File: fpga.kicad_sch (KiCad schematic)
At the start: 10 parts, among them U10 P0082_BOTTOMMOUNT, Y1 XLL735080.000000I

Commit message: Start working on ERC, properly annotate DNP elements
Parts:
- R56, R58, R72: now not fitted
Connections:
- no-connect marks 1 -> 22
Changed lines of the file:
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@@
 	)
 	(no_connect
+		(at 125.73 95.25)
+	)
+	(no_connect
+		(at 125.73 135.89)
+	)
+	(no_connect
+		(at 125.73 128.27)
+	)
+	(no_connect
+		(at 80.01 49.53)
+	)
+	(no_connect
+		(at 125.73 130.81)
+	)
+	(no_connect
+		(at 80.01 100.33)
+	)
+	(no_connect
+		(at 125.73 90.17)
+	)
+	(no_connect
 		(at 217.17 59.69)
 	)
+	(no_connect
+		(at 125.73 92.71)
+	)
+	(no_connect
+		(at 125.73 87.63)
+	)
+	(no_connect
+		(at 125.73 120.65)
+	)
+	(no_connect
+		(at 80.01 90.17)
+	)
+	(no_connect
+		(at 80.01 46.99)
+	)
+	(no_connect
+		(at 125.73 123.19)
+	)
+	(no_connect
+		(at 125.73 62.23)
+	)
+	(no_connect
+		(at 80.01 123.19)
+	)
+	(no_connect
+		(at 80.01 92.71)
+	)
+	(no_connect
+		(at 125.73 64.77)
+	)
+	(no_connect
+		(at 125.73 46.99)
+	)
+	(no_connect
+		(at 125.73 125.73)
+	)
+	(no_connect
+		(at 80.01 95.25)
+	)
+	(no_connect
+		(at 125.73 85.09)
+	)
 	(bus_entry
 		(at 181.61 106.68)
@@
 		(in_bom yes)
 		(on_board yes)
-		(dnp no)
+		(dnp yes)
 		(fields_autoplaced yes)
 		(property "Reference" "R72"
@@
 		(in_bom yes)
 		(on_board yes)
-		(dnp no)
+		(dnp yes)
 		(property "Reference" "R56"
 			(at 138.176 40.64 90)
@@
 		(in_bom yes)
 		(on_board yes)
-		(dnp no)
+		(dnp yes)
 		(property "Reference" "R58"
 			(at 138.176 114.3 90)

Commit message: Fix ERC
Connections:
- net +3.3V is gone; now on net +3V3: C140.1, R72.1, Y1.6 (VDD)
- net ADC_B_10: no longer U10.JP2_33 (GPIO_126)
- net ADC_B_11: no longer U10.JP2_35 (GPIO_128)
- net OVERFLOW: now reaches U10.JP1_35 (GPIO_028)
- new net ADC_B_12: U10.JP2_33 (GPIO_126)
- new net ADC_B_13: U10.JP2_35 (GPIO_128)
- no-connect marks 22 -> 21
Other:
- moved on the sheet: R55, R56, R57, R58, R72

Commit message: Add all footprints
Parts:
- renumbered C140 to C100, R180 to R58, R181 to R59, R55 to R60, R56 to R61, R57 to R62, R58 to R63, R72 to R64
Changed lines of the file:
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@@
 		(on_board yes)
 		(dnp no)
-		(property "Reference" "R181"
+		(property "Reference" "R59"
 			(at 70.866 86.36 90)
 			(effects
@@
 			(project "DigitalOsciloscope"
 				(path "/553deb7b-4100-40fe-99d2-0c7b4b56aad2/3a7288c4-cf21-495b-9b8e-7b87b52ff1d8"
-					(reference "R181")
+					(reference "R59")
 					(unit 1)
 				)
@@
 		(dnp no)
 		(fields_autoplaced yes)
-		(property "Reference" "#PWR056"
+		(property "Reference" "#PWR0143"
 			(at 161.29 41.91 0)
 			(effects
@@
 			(project "DigitalOsciloscope"
 				(path "/553deb7b-4100-40fe-99d2-0c7b4b56aad2/3a7288c4-cf21-495b-9b8e-7b87b52ff1d8"
-					(reference "#PWR056")
+					(reference "#PWR0143")
 					(unit 1)
 				)
@@
 		(dnp no)
 		(fields_autoplaced yes)
-		(property "Reference" "#PWR0243"
+		(property "Reference" "#PWR0148"
 			(at 236.22 72.39 0)
 			(effects
@@
 			(project ""
 				(path "/553deb7b-4100-40fe-99d2-0c7b4b56aad2/3a7288c4-cf21-495b-9b8e-7b87b52ff1d8"
-					(reference "#PWR0243")
+					(reference "#PWR0148")
 					(unit 1)
 				)
@@
 		(dnp no)
 		(fields_autoplaced yes)
-		(property "Reference" "#PWR054"
+		(property "Reference" "#PWR0144"
 			(at 161.29 115.57 0)
 			(effects
@@
 			(project ""
 				(path "/553deb7b-4100-40fe-99d2-0c7b4b56aad2/3a7288c4-cf21-495b-9b8e-7b87b52ff1d8"
-					(reference "#PWR054")
+					(reference "#PWR0144")
 					(unit 1)
 				)
@@
 		(on_board yes)
 		(dnp no)
-		(property "Reference" "R180"
+		(property "Reference" "R58"
 			(at 70.866 83.82 90)
 			(effects
@@
 			(project "DigitalOsciloscope"
 				(path "/553deb7b-4100-40fe-99d2-0c7b4b56aad2/3a7288c4-cf21-495b-9b8e-7b87b52ff1d8"
-					(reference "R180")
+					(reference "R58")
 					(unit 1)
 				)
@@
 		(dnp no)
 		(fields_autoplaced yes)
-		(property "Reference" "#PWR0160"
+		(property "Reference" "#PWR0145"
 			(at 176.53 58.42 0)
 			(effects
@@
 			(project "DigitalOsciloscope"
 				(path "/553deb7b-4100-40fe-99d2-0c7b4b56aad2/3a7288c4-cf21-495b-9b8e-7b87b52ff1d8"
-					(reference "#PWR0160")
+					(reference "#PWR0145")
 					(unit 1)
 				)
@@
 		(dnp no)
 		(fields_autoplaced yes)
-		(property "Reference" "#FLG034"
+		(property "Reference" "#FLG024"
 			(at 134.62 111.125 0)
 			(effects
@@
 			(project "DigitalOsciloscope"
 				(path "/553deb7b-4100-40fe-99d2-0c7b4b56aad2/3a7288c4-cf21-495b-9b8e-7b87b52ff1d8"
-					(reference "#FLG034")
+					(reference "#FLG024")
 					(unit 1)
 				)
@@
 		(dnp no)
 		(fields_autoplaced yes)
-		(property "Reference" "#PWR053"
+		(property "Reference" "#PWR0142"
 			(at 156.21 115.57 0)
 			(effects
@@
 			(project ""
 				(path "/553deb7b-4100-40fe-99d2-0c7b4b56aad2/3a7288c4-cf21-495b-9b8e-7b87b52ff1d8"
-					(reference "#PWR053")
+					(reference "#PWR0142")
 					(unit 1)
 				)
@@
 		(dnp yes)
 		(fields_autoplaced yes)
-		(property "Reference" "R72"
+		(property "Reference" "R64"
 			(at 182.88 50.8 90)
 			(effects
@@
 			(project ""
 				(path "/553deb7b-4100-40fe-99d2-0c7b4b56aad2/3a7288c4-cf21-495b-9b8e-7b87b52ff1d8"
-					(reference "R72")
+					(reference "R64")
 					(unit 1)
 				)
@@
 		(dnp no)
 		(fields_autoplaced yes)
-		(property "Reference" "#PWR057"
+		(property "Reference" "#PWR0140"
 			(at 127 185.42 0)
 			(effects
@@
 			(project ""
 				(path "/553deb7b-4100-40fe-99d2-0c7b4b56aad2/3a7288c4-cf21-495b-9b8e-7b87b52ff1d8"
-					(reference "#PWR057")
+					(reference "#PWR0140")
 					(unit 1)
 				)
@@
 		(on_board yes)
 		(dnp no)
-		(property "Reference" "#FLG06"
+		(property "Reference" "#FLG023"
 			(at 134.62 43.815 0)
 			(effects
@@
 			(project "DigitalOsciloscope"
 				(path "/553deb7b-4100-40fe-99d2-0c7b4b56aad2/3a7288c4-cf21-495b-9b8e-7b87b52ff1d8"
-					(reference "#FLG06")
+					(reference "#FLG023")
 					(unit 1)
 				)
@@
 		(dnp no)
 		(fields_autoplaced yes)
-		(property "Reference" "#FLG035"
+		(property "Reference" "#FLG025"
 			(at 134.62 117.475 0)
 			(effects
@@
 			(project "DigitalOsciloscope"
 				(path "/553deb7b-4100-40fe-99d2-0c7b4b56aad2/3a7288c4-cf21-495b-9b8e-7b87b52ff1d8"
-					(reference "#FLG035")
+					(reference "#FLG025")
 					(unit 1)
 				)
@@
 		(dnp no)
 		(fields_autoplaced yes)
-		(property "Reference" "#PWR0244"
+		(property "Reference" "#PWR0146"
 			(at 187.96 69.85 0)
 			(effects
@@
 			(project "DigitalOsciloscope"
 				(path "/553deb7b-4100-40fe-99d2-0c7b4b56aad2/3a7288c4-cf21-495b-9b8e-7b87b52ff1d8"
-					(reference "#PWR0244")
+					(reference "#PWR0146")
 					(unit 1)
 				)
@@
 		(dnp no)
 		(fields_autoplaced yes)
-		(property "Reference" "#PWR058"
+		(property "Reference" "#PWR0139"
 			(at 127 109.22 0)
 			(effects
@@
 			(project "DigitalOsciloscope"
 				(path "/553deb7b-4100-40fe-99d2-0c7b4b56aad2/3a7288c4-cf21-495b-9b8e-7b87b52ff1d8"
-					(reference "#PWR058")
+					(reference "#PWR0139")
 					(unit 1)
 				)
@@
 		(on_board yes)
 		(dnp no)
-		(property "Reference" "R55"
+		(property "Reference" "R60"
 			(at 148.336 38.1 90)
 			(effects
@@
 			(project "DigitalOsciloscope"
 				(path "/553deb7b-4100-40fe-99d2-0c7b4b56aad2/3a7288c4-cf21-495b-9b8e-7b87b52ff1d8"
-					(reference "R55")
+					(reference "R60")
 					(unit 1)
 				)
@@
 		(dnp no)
 		(fields_autoplaced yes)
-		(property "Reference" "#PWR059"
+		(property "Reference" "#PWR0147"
 			(at 236.22 58.42 0)
 			(effects
@@
 			(project "DigitalOsciloscope"
 				(path "/553deb7b-4100-40fe-99d2-0c7b4b56aad2/3a7288c4-cf21-495b-9b8e-7b87b52ff1d8"
-					(reference "#PWR059")
+					(reference "#PWR0147")
 					(unit 1)
 				)
@@
 		(dnp no)
 		(fields_autoplaced yes)
-		(property "Reference" "#PWR055"
+		(property "Reference" "#PWR0141"
 			(at 156.21 41.91 0)
 			(effects
@@
 			(project "DigitalOsciloscope"
 				(path "/553deb7b-4100-40fe-99d2-0c7b4b56aad2/3a7288c4-cf21-495b-9b8e-7b87b52ff1d8"
-					(reference "#PWR055")
+					(reference "#PWR0141")
 					(unit 1)
 				)
@@
 		(on_board yes)
 		(dnp no)
-		(property "Reference" "R57"
+		(property "Reference" "R62"
 			(at 148.336 111.76 90)
 			(effects
@@
 			(project "DigitalOsciloscope"
 				(path "/553deb7b-4100-40fe-99d2-0c7b4b56aad2/3a7288c4-cf21-495b-9b8e-7b87b52ff1d8"
-					(reference "R57")
+					(reference "R62")
 					(unit 1)
 				)
@@
 		(dnp no)
 		(fields_autoplaced yes)
-		(property "Reference" "#FLG05"
+		(property "Reference" "#FLG022"
 			(at 134.62 37.465 0)
 			(effects
@@
 			(project ""
 				(path "/553deb7b-4100-40fe-99d2-0c7b4b56aad2/3a7288c4-cf21-495b-9b8e-7b87b52ff1d8"
-					(reference "#FLG05")
+					(reference "#FLG022")
 					(unit 1)
 				)
@@
 		(on_board yes)
 		(dnp yes)
-		(property "Reference" "R56"
+		(property "Reference" "R61"
 			(at 148.336 40.64 90)
 			(effects
@@
 			(project "DigitalOsciloscope"
 				(path "/553deb7b-4100-40fe-99d2-0c7b4b56aad2/3a7288c4-cf21-495b-9b8e-7b87b52ff1d8"
-					(reference "R56")
+					(reference "R61")
 					(unit 1)
 				)
@@
 		(on_board yes)
 		(dnp yes)
-		(property "Reference" "R58"
+		(property "Reference" "R63"
 			(at 148.336 114.3 90)
 			(effects
@@
 			(project "DigitalOsciloscope"
 				(path "/553deb7b-4100-40fe-99d2-0c7b4b56aad2/3a7288c4-cf21-495b-9b8e-7b87b52ff1d8"
-					(reference "R58")
+					(reference "R63")
 					(unit 1)
 				)
@@
 		(dnp no)
 		(fields_autoplaced yes)
-		(property "Reference" "C140"
+		(property "Reference" "C100"
 			(at 240.03 60.9599 0)
 			(effects
@@
 			(project ""
 				(path "/553deb7b-4100-40fe-99d2-0c7b4b56aad2/3a7288c4-cf21-495b-9b8e-7b87b52ff1d8"
-					(reference "C140")
-					(unit 1)
-				)
+					(reference "C100")
+					(unit 1)
+				)

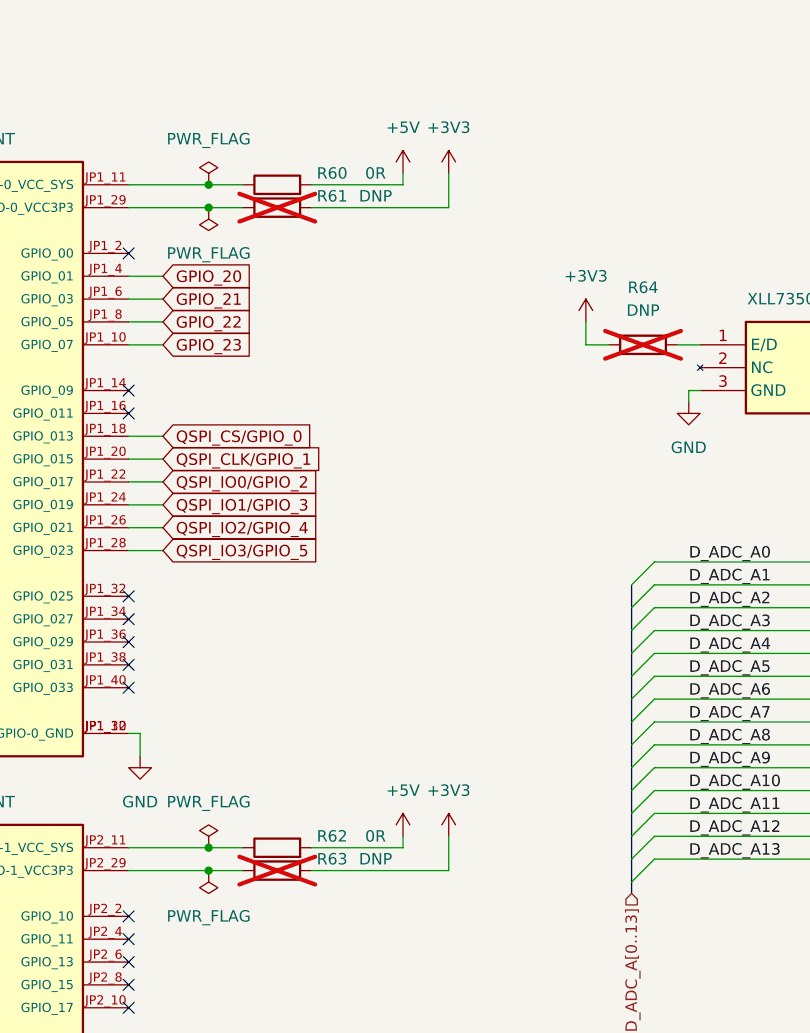
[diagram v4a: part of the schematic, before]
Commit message: Apply changes after review, left to fix: comparator histeresis, PSU missing lines?
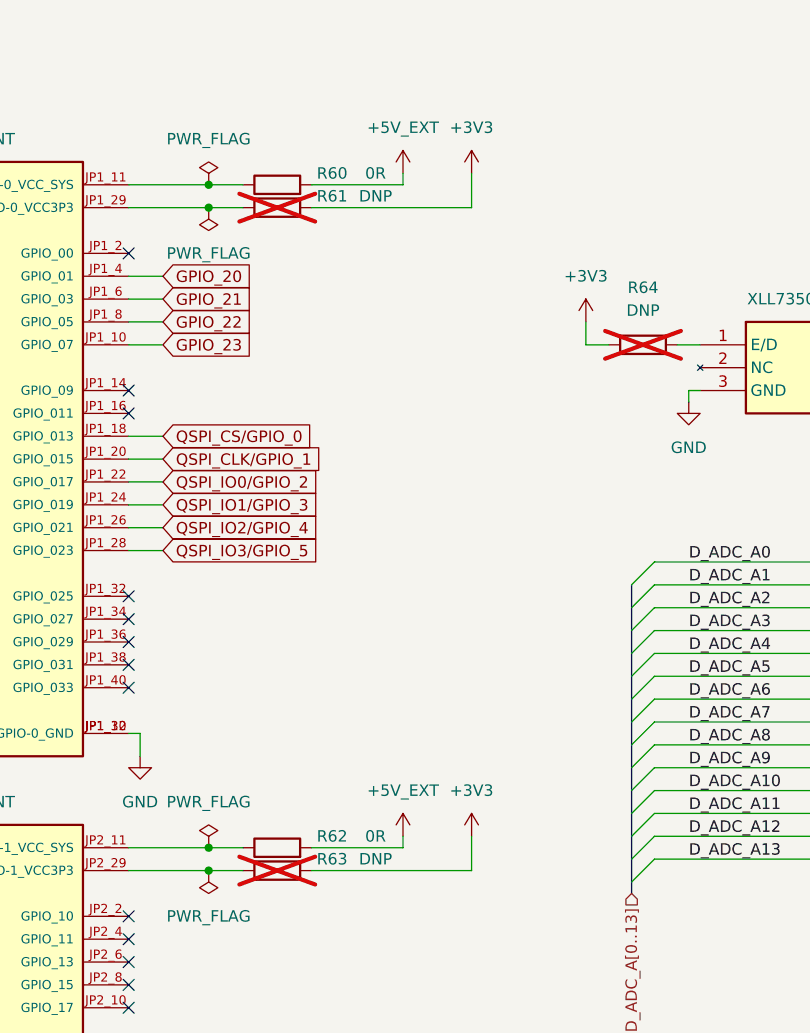
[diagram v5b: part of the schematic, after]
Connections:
- net +5V renamed +5V_EXT
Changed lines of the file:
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@@
 	(wire
 		(pts
-			(xy 161.29 111.76) (xy 161.29 115.57)
+			(xy 163.83 111.76) (xy 163.83 115.57)
 		)
 		(stroke
@@
 	(wire
 		(pts
-			(xy 161.29 115.57) (xy 146.05 115.57)
+			(xy 163.83 115.57) (xy 146.05 115.57)
 		)
 		(stroke
@@
 	(wire
 		(pts
-			(xy 161.29 38.1) (xy 161.29 41.91)
+			(xy 163.83 38.1) (xy 163.83 41.91)
 		)
 		(stroke
@@
 	(wire
 		(pts
-			(xy 161.29 41.91) (xy 146.05 41.91)
+			(xy 163.83 41.91) (xy 146.05 41.91)
 		)
 		(stroke
@@
 	(symbol
 		(lib_id "power:+3V3")
-		(at 161.29 38.1 0)
+		(at 163.83 38.1 0)
 		(unit 1)
 		(exclude_from_sim no)
@@
 		(fields_autoplaced yes)
 		(property "Reference" "#PWR0143"
-			(at 161.29 41.91 0)
+			(at 163.83 41.91 0)
 			(effects
 				(font
@@
 		)
 		(property "Value" "+3V3"
-			(at 161.29 33.02 0)
+			(at 163.83 33.02 0)
 			(effects
 				(font
@@
 		)
 		(property "Footprint" ""
-			(at 161.29 38.1 0)
+			(at 163.83 38.1 0)
 			(effects
 				(font
@@
 		)
 		(property "Datasheet" ""
-			(at 161.29 38.1 0)
+			(at 163.83 38.1 0)
 			(effects
 				(font
@@
 		)
 		(property "Description" "Power symbol creates a global label with name \"+3V3\""
-			(at 161.29 38.1 0)
+			(at 163.83 38.1 0)
 			(effects
 				(font
@@
 	(symbol
 		(lib_id "power:+3V3")
-		(at 161.29 111.76 0)
+		(at 163.83 111.76 0)
 		(unit 1)
 		(exclude_from_sim no)
@@
 		(fields_autoplaced yes)
 		(property "Reference" "#PWR0144"
-			(at 161.29 115.57 0)
+			(at 163.83 115.57 0)
 			(effects
 				(font
@@
 		)
 		(property "Value" "+3V3"
-			(at 161.29 106.68 0)
+			(at 163.83 106.68 0)
 			(effects
 				(font
@@
 		)
 		(property "Footprint" ""
-			(at 161.29 111.76 0)
+			(at 163.83 111.76 0)
 			(effects
 				(font
@@
 		)
 		(property "Datasheet" ""
-			(at 161.29 111.76 0)
+			(at 163.83 111.76 0)
 			(effects
 				(font
@@
 		)
 		(property "Description" "Power symbol creates a global label with name \"+3V3\""
-			(at 161.29 111.76 0)
+			(at 163.83 111.76 0)
 			(effects
 				(font
@@
 	)
 	(symbol
-		(lib_id "power:+5V")
-		(at 156.21 111.76 0)
-		(unit 1)
-		(exclude_from_sim no)
-		(in_bom yes)
-		(on_board yes)
-		(dnp no)
-		(fields_autoplaced yes)
-		(property "Reference" "#PWR0142"
-			(at 156.21 115.57 0)
-			(effects
-				(font
-					(size 1.27 1.27)
-				)
-				(hide yes)
-			)
-		)
-		(property "Value" "+5V"
-			(at 156.21 106.68 0)
-			(effects
-				(font
-					(size 1.27 1.27)
-				)
-			)
-		)
-		(property "Footprint" ""
-			(at 156.21 111.76 0)
-			(effects
-				(font
-					(size 1.27 1.27)
-				)
-				(hide yes)
-			)
-		)
-		(property "Datasheet" ""
-			(at 156.21 111.76 0)
-			(effects
-				(font
-					(size 1.27 1.27)
-				)
-				(hide yes)
-			)
-		)
-		(property "Description" "Power symbol creates a global label with name \"+5V\""
-			(at 156.21 111.76 0)
-			(effects
-				(font
-					(size 1.27 1.27)
-				)
-				(hide yes)
-			)
-		)
-		(pin "1"
-		)
-		(instances
-			(project ""
-				(path "/553deb7b-4100-40fe-99d2-0c7b4b56aad2/3a7288c4-cf21-495b-9b8e-7b87b52ff1d8"
-					(reference "#PWR0142")
-					(unit 1)
-				)
-			)
-		)
-	)
-	(symbol
 		(lib_id "Device:R")
 		(at 182.88 57.15 90)
@@
 	)
 	(symbol
-		(lib_id "power:+5V")
-		(at 156.21 38.1 0)
+		(lib_id "+2v5:+5V_EXT")
+		(at 156.21 111.76 0)
 		(unit 1)
 		(exclude_from_sim no)
@@
 		(fields_autoplaced yes)
 		(property "Reference" "#PWR0141"
-			(at 156.21 41.91 0)
+			(at 156.21 115.57 0)
 			(effects
 				(font
@@
 			)
 		)
-		(property "Value" "+5V"
-			(at 156.21 33.02 0)
+		(property "Value" "+5V_EXT"
+			(at 156.21 106.68 0)
 			(effects
 				(font
@@
 		)
 		(property "Footprint" ""
-			(at 156.21 38.1 0)
+			(at 156.21 111.76 0)
 			(effects
 				(font
@@
 		)
 		(property "Datasheet" ""
-			(at 156.21 38.1 0)
+			(at 156.21 111.76 0)
 			(effects
 				(font
@@
 			)
 		)
-		(property "Description" "Power symbol creates a global label with name \"+5V\""
-			(at 156.21 38.1 0)
+		(property "Description" "Power symbol creates a global label with name \"+6V5\""
+			(at 156.21 111.76 0)
 			(effects
 				(font
@@
 					(unit 1)
 				)
+			)
+		)
+	)
+	(symbol
+		(lib_id "+2v5:+5V_EXT")
+		(at 156.21 38.1 0)
+		(unit 1)
+		(exclude_from_sim no)
+		(in_bom yes)
+		(on_board yes)
+		(dnp no)
+		(fields_autoplaced yes)
+		(property "Reference" "#PWR0107"
+			(at 156.21 41.91 0)
+			(effects
+				(font
+					(size 1.27 1.27)
+				)
+				(hide yes)
+			)
+		)
+		(property "Value" "+5V_EXT"
+			(at 156.21 33.02 0)
+			(effects
+				(font
+					(size 1.27 1.27)
+				)
+			)
+		)
+		(property "Footprint" ""
+			(at 156.21 38.1 0)
+			(effects
+				(font
+					(size 1.27 1.27)
+				)
+				(hide yes)
+			)
+		)
+		(property "Datasheet" ""
+			(at 156.21 38.1 0)
+			(effects
+				(font
+					(size 1.27 1.27)
+				)
+				(hide yes)
+			)
+		)
+		(property "Description" "Power symbol creates a global label with name \"+6V5\""
+			(at 156.21 38.1 0)
+			(effects
+				(font
+					(size 1.27 1.27)
+				)
+				(hide yes)
+			)
+		)
+		(pin "1"
+		)
+		(instances
+			(project ""
+				(path "/553deb7b-4100-40fe-99d2-0c7b4b56aad2/3a7288c4-cf21-495b-9b8e-7b87b52ff1d8"
+					(reference "#PWR0107")
+					(unit 1)
+				)
